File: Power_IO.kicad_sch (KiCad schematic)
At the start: 24 parts, among them J10 Power_IO_JMP, M3 MOSFET_SI7155DP-T1-GE3

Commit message: Update
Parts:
- removed R45, R54, R55, R56: 0.05R, Resistor_SMD:R_0805_2012Metric, symbol Device:R
- removed R46, R47, R48, R49, R57, R58, R59, R60: 0R, Resistor_SMD:R_0805_2012Metric, symbol Device:R
- added D6: MMSZ5241BQ-7-F, Diode_SMD:D_SOD-123, symbol Device:D_Zener
- added M1: MOSFET_SI7155DP-T1-GE3, Personal_Project:MOSFET_SI7155DPT1GE3, symbol Personal_Projects:MOSFET_SI7155DP-T1-GE3
- added R1: 100K, Resistor_SMD:R_0805_2012Metric, symbol Device:R
- added R2: 10K, Resistor_SMD:R_0805_2012Metric, symbol Device:R
- added S2: Switch_WS-SLSU SMT Mini Slide, Personal_Project:Switch_WS-SLSU SMT Mini Slide, symbol Personal_Projects:Switch_WS-SLSU SMT Mini Slide
- D1: footprint Diode_SMD:D_SOD-128 -> Diode_SMD:D_SOD-123
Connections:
- net +VIN_SMPS: now also M1.5 (D); no longer D1.1 (K), J10.2 (Pin_2), J10.4 (Pin_4), J10.6 (Pin_6), J10.8 (Pin_8)
- net GND: now also S2.3, S2.MP1, S2.MP2, S2.MP3, S2.MP4
- net PWR+: no longer M3.6 (D), M3.7 (D), M3.8 (D)
- net CONN1+: now reaches CONN2.A, J10.1 (Pin_1)
- net CONN2+: now reaches CONN1.A, J10.3 (Pin_3)
- new net: R2.2, S2.1
- new net +VIN_S: D1.1 (K), D6.1 (K), J10.2 (Pin_2), J10.4 (Pin_4), J10.6 (Pin_6), J10.8 (Pin_8), M1.1 (S), M1.2 (S), M1.3 (S), R1.2
- new net ONF_GATE: D6.2 (A), M1.4 (G), R1.1, R2.1
- no-connect marks 0 -> 1
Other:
- moved on the sheet: CONN1, CONN2, D1, D3, J10, JST1, JST2, JST3, JST4, JST5, M3, R22

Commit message: Update
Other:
- company: (none) -> Peter Hancak
- title: (none) -> USB-PD Board
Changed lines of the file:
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@@
 	(generator_version "8.0")
 	(paper "USLetter")
+	(title_block
+		(title "USB-PD Board")
+		(date "2025-12-03")
+		(rev "B")
+		(company "Peter Hancak")
+	)
 	(junction
 		(at 179.07 73.66)
@@
 	(wire
 		(pts
-			(xy 73.66 176.53) (xy 113.03 176.53)
+			(xy 73.66 176.53) (xy 111.76 176.53)
 		)
 		(stroke
@@
 	(wire
 		(pts
-			(xy 113.03 107.95) (xy 113.03 176.53)
+			(xy 111.76 107.95) (xy 111.76 176.53)
 		)
 		(stroke
@@
 	(wire
 		(pts
-			(xy 113.03 107.95) (xy 133.35 107.95)
-		)
-		(stroke
+			(xy 111.76 107.95) (xy 133.35 107.95)
+		)
+		(stroke

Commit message: Update
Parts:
- added C1: 100n, Capacitor_SMD:C_0805_2012Metric, symbol Device:C
- R1: value 100K -> 10K
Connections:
- net +VIN_SMPS: now also C1.1
- net ONF_GATE: now also C1.2
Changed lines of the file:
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@@
 	)
 	(junction
+		(at 200.66 124.46)
+		(diameter 0)
+		(color 0 0 0 0)
+	)
+	(junction
 		(at 200.66 128.27)
 		(diameter 0)
@@
 	)
 	(junction
+		(at 222.25 105.41)
+		(diameter 0)
+		(color 0 0 0 0)
+	)
+	(junction
 		(at 134.62 73.66)
 		(diameter 0)
@@
 	(wire
 		(pts
-			(xy 200.66 118.11) (xy 200.66 128.27)
+			(xy 200.66 118.11) (xy 200.66 124.46)
 		)
 		(stroke
@@
 	(wire
 		(pts
+			(xy 222.25 119.38) (xy 222.25 124.46)
+		)
+		(stroke
+			(width 0)
+			(type default)
+		)
+	)
+	(wire
+		(pts
 			(xy 71.12 35.56) (xy 71.12 33.02)
 		)
@@
 	(wire
 		(pts
-			(xy 213.36 105.41) (xy 248.92 105.41)
+			(xy 213.36 105.41) (xy 222.25 105.41)
 		)
 		(stroke
@@
 	(wire
 		(pts
+			(xy 222.25 111.76) (xy 222.25 105.41)
+		)
+		(stroke
+			(width 0)
+			(type default)
+		)
+	)
+	(wire
+		(pts
 			(xy 106.68 113.03) (xy 133.35 113.03)
 		)
@@
 	(wire
 		(pts
+			(xy 200.66 124.46) (xy 200.66 128.27)
+		)
+		(stroke
+			(width 0)
+			(type default)
+		)
+	)
+	(wire
+		(pts
 			(xy 123.19 52.07) (xy 127 52.07)
 		)
@@
 	(wire
 		(pts
+			(xy 222.25 124.46) (xy 200.66 124.46)
+		)
+		(stroke
+			(width 0)
+			(type default)
+		)
+	)
+	(wire
+		(pts
 			(xy 172.72 50.8) (xy 172.72 60.96)
 		)
@@
 	(wire
 		(pts
+			(xy 222.25 105.41) (xy 248.92 105.41)
+		)
+		(stroke
+			(width 0)
+			(type default)
+		)
+	)
+	(wire
+		(pts
 			(xy 109.22 110.49) (xy 109.22 148.59)
 		)
@@
 	)
 	(symbol
+		(lib_id "Device:C")
+		(at 222.25 115.57 0)
+		(unit 1)
+		(exclude_from_sim no)
+		(in_bom yes)
+		(on_board yes)
+		(dnp no)
+		(property "Reference" "C1"
+			(at 223.266 113.284 0)
+			(effects
+				(font
+					(size 1.27 1.27)
+				)
+				(justify left)
+			)
+		)
+		(property "Value" "100n"
+			(at 223.266 118.11 0)
+			(effects
+				(font
+					(size 1.27 1.27)
+				)
+				(justify left)
+			)
+		)
+		(property "Footprint" "Capacitor_SMD:C_0805_2012Metric"
+			(at 223.2152 119.38 0)
+			(effects
+				(font
+					(size 1.27 1.27)
+				)
+				(hide yes)
+			)
+		)
+		(property "Datasheet" "~"
+			(at 222.25 115.57 0)
+			(effects
+				(font
+					(size 1.27 1.27)
+				)
+				(hide yes)
+			)
+		)
+		(property "Description" "Unpolarized capacitor"
+			(at 222.25 115.57 0)
+			(effects
+				(font
+					(size 1.27 1.27)
+				)
+				(hide yes)
+			)
+		)
+		(pin "1"
+		)
+		(pin "2"
+		)
+		(instances
+			(project "USBPD_Board"
+				(path "/b3855754-13ea-49fc-935d-9d42ea1a9383/8ca2a2be-b278-4705-baff-3e3f01daf622"
+					(reference "C1")
+					(unit 1)
+				)
+			)
+		)
+	)
+	(symbol
 		(lib_id "Personal_Projects:CONN_54-00166")
 		(at 68.58 151.13 0)
@@
 			)
 		)
-		(property "Value" "100K"
+		(property "Value" "10K"
 			(at 172.72 111.252 90)
 			(effects

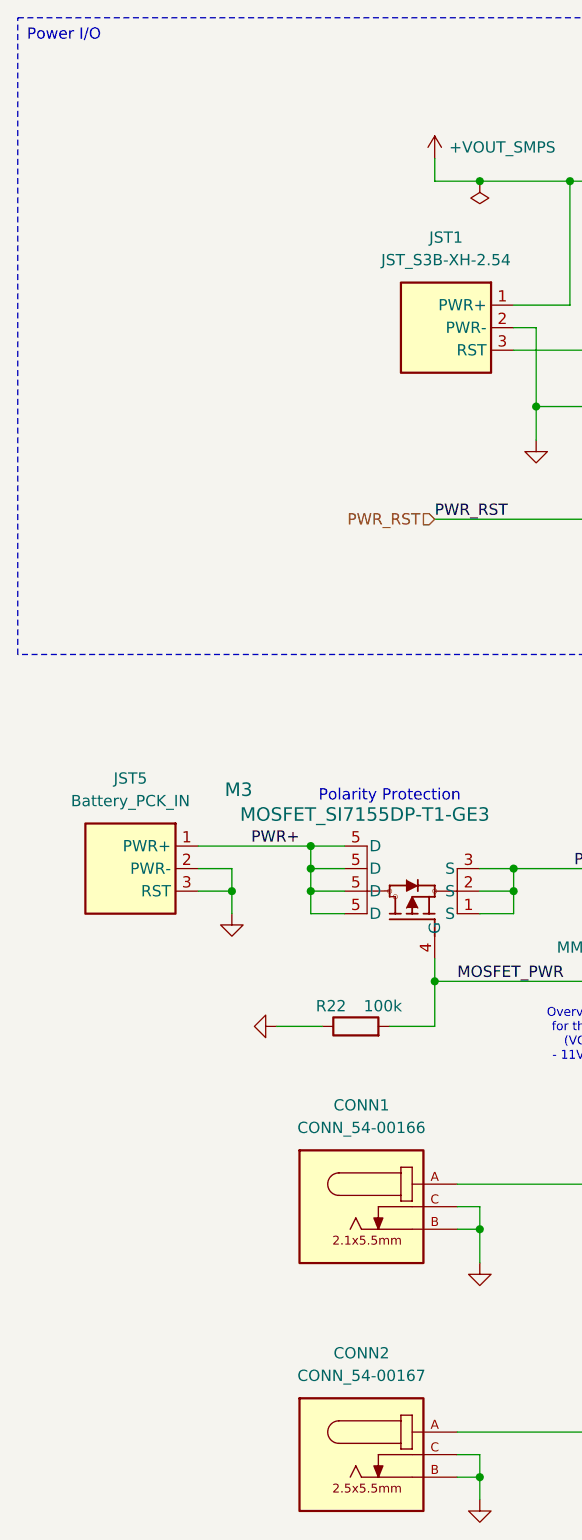
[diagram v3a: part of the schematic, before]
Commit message: Change Kicad version
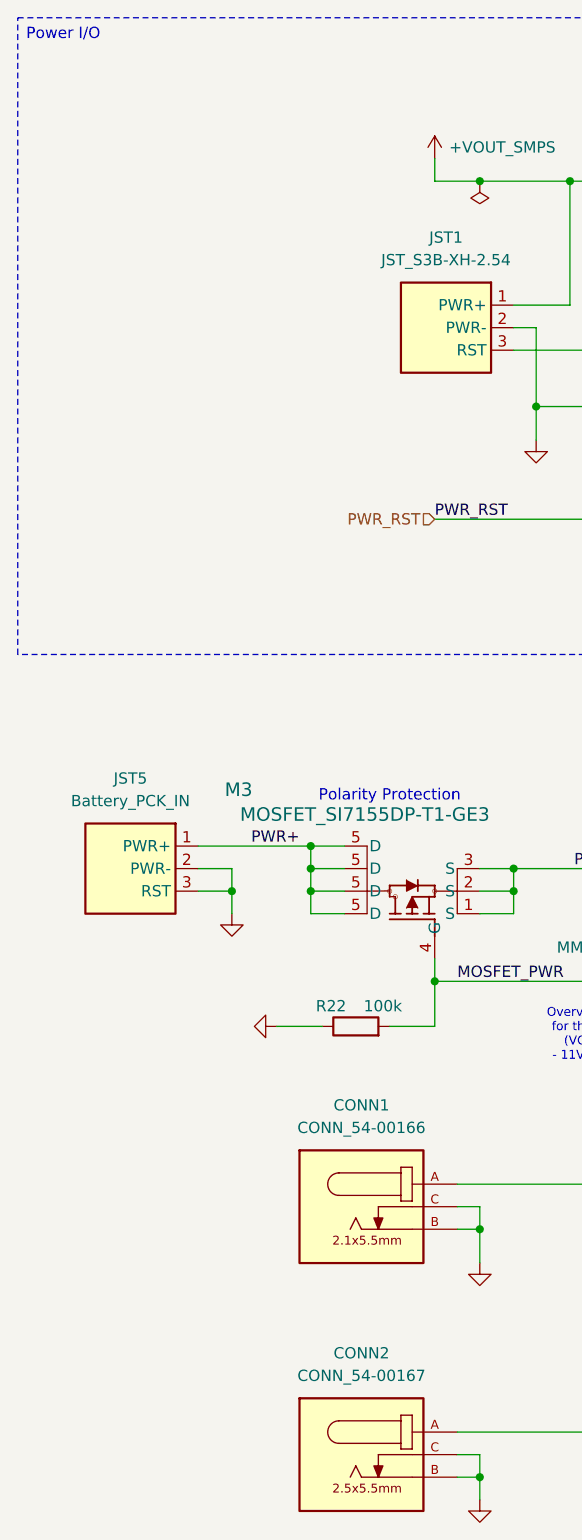
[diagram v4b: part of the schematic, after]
